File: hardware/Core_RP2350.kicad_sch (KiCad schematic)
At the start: 71 parts, among them J1 5-146281-3, J2 5-146281-3, J3 AudioJack3, J4 USB_C_Receptacle_USB2.0, J5 Micro_SD_Card_Det_Hirose_DM3AT, SW1 SPST-NO, SW2 SPST-NO, SW3 SPST-NO, U2 W25Q16JVUXIQ, U3 ADUM4160, U32 RP2350_80QFN

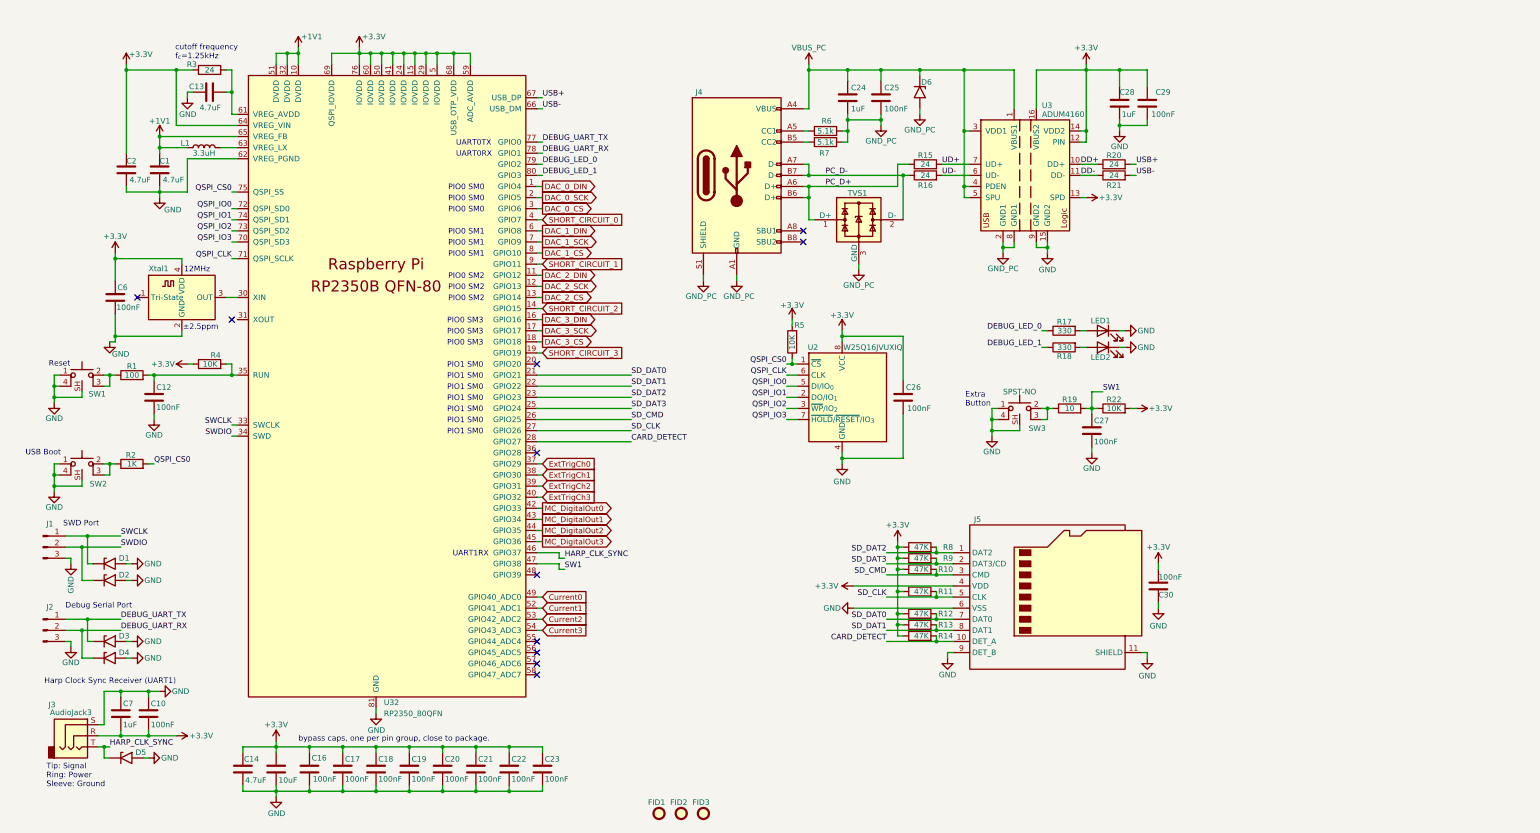
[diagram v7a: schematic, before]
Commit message: draft power pours in internal layers
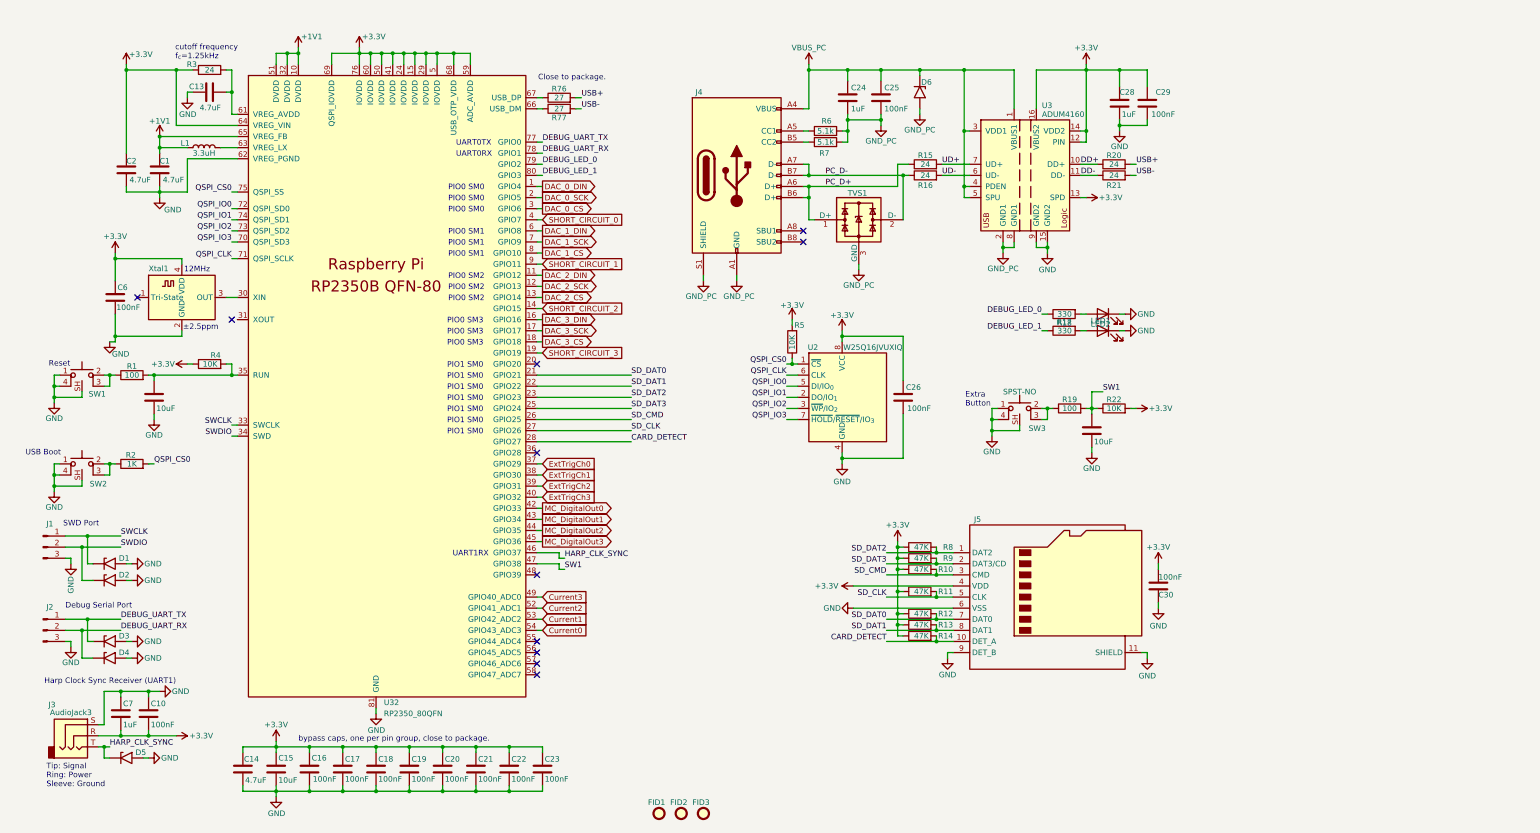
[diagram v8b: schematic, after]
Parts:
- removed C12, C27: 100nF, Capacitor_SMD:C_0402_1005Metric, symbol harp.device.quad.dac:C_0603
- added C3, C4: 10uF, Capacitor_SMD:C_0603_1608Metric, symbol harp.device.quad.dac:C_0603
- added R76, R77: 27, Resistor_SMD:R_0402_1005Metric, symbol Device:R
- LED1, LED2: footprint harp.device.quad.dac.kicad:LED_0603_1608Metric_Pad1.05x0.95mm_HandSolder -> LED_SMD:LED_0603_1608Metric_Pad1.05x0.95mm_HandSolder
- R19: value 10 -> 100; footprint Resistor_SMD:R_0402_1005Metric -> Resistor_SMD:R_0603_1608Metric; Link https://www.digikey.com/en/products/detail/yageo/AC0603FR-1310RL/17006001 -> https://www.digikey.com/en/products/detail/yageo/AC0603FR-13100RL/12756385; Manufacturer (none) -> Yageo; Manufacturer Number (none) -> RT0402BRD071KL
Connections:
- net Current0: now also U32.54 (GPIO43_ADC3); no longer U32.49 (GPIO40_ADC0)
- net Current1: now also U32.53 (GPIO42_ADC2); no longer U32.52 (GPIO41_ADC1)
- net Current2: now also U32.52 (GPIO41_ADC1); no longer U32.53 (GPIO42_ADC2)
- net Current3: now also U32.49 (GPIO40_ADC0); no longer U32.54 (GPIO43_ADC3)
- net DEBUG_LED_0: now also R18.1; no longer R17.1
- net DEBUG_LED_1: now also R17.1; no longer R18.1
- net GND: now also C3.2, C4.2
- net SW1: now also C4.1
- net USB+: now also R76.2; no longer U32.67 (USB_DP)
- net USB-: now also R77.2; no longer U32.66 (USB_DM)
- net at R1.2, R4.2, U32.35 (RUN): now also C3.1
- new net: R77.1, U32.66 (USB_DM)
- new net: R76.1, U32.67 (USB_DP)
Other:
- note added: "Close to package."
- moved on the sheet: LED2, R18
